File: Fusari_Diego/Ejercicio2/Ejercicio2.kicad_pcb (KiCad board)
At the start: 2 copper layers, 40.6 x 61 mm, 15 parts, among them J1 DB9, U1 AMIS42665TJAA1RG, U2 SP3232_V2

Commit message: Se agregan los archivos pcb con 3d
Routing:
- net GND: track 0.13 -> 20.2 mm, vias 0 -> 2
- added copper zone on B.Cu, net GND
- added copper zone on F.Cu, net GND
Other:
- board text added: "INDUSTRIA ARGENTINA"
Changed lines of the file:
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@@
   (general
     (links 43)
-    (no_connects 18)
+    (no_connects 0)
     (area 99.670799 78.664999 140.460801 139.775001)
     (thickness 1.6)
-    (drawings 4)
-    (tracks 205)
+    (drawings 5)
+    (tracks 215)
     (zones 0)
     (modules 15)
@@
     (user_trace_width 0.3048)
     (trace_clearance 0.3048)
-    (zone_clearance 0.508)
+    (zone_clearance 0.3048)
     (zone_45_only no)
     (trace_min 0.2)
@@
     (pad 2 smd rect (at 2 0) (size 2 1.7) (layers F.Cu F.Paste F.Mask)
       (net 20 "Net-(R1-Pad2)"))
-    (model Resistors_SMD.3dshapes/R_1206_HandSoldering.wrl
+    (model ${KIPRJMOD}/ej2.3dshapes/R_1206_HandSoldering.wrl
       (at (xyz 0 0 0))
       (scale (xyz 1 1 1))
@@
     (pad 2 smd rect (at 2 0) (size 2 1.7) (layers F.Cu F.Paste F.Mask)
       (net 10 "Net-(CAN1-Pad2)"))
-    (model Resistors_SMD.3dshapes/R_1206_HandSoldering.wrl
+    (model ${KIPRJMOD}/ej2.3dshapes/R_1206_HandSoldering.wrl
       (at (xyz 0 0 0))
       (scale (xyz 1 1 1))
@@
     (pad 16 smd rect (at -4.445 -2.59842 270) (size 0.59944 2.19964) (layers F.Cu F.Paste F.Mask)
       (net 9 +3.3V))
-    (model ${KIPRJMOD}/ej2.3dshapes/so-16.wrl
+    (model ${KIPRJMOD}/ej2.3dshapes/soic-16.wrl
       (at (xyz 0 0 0))
       (scale (xyz 1 1 1))
@@
     (pad 2 smd rect (at 2.032 0 270) (size 2 1.6) (layers F.Cu F.Paste F.Mask)
       (net 2 "Net-(C1-Pad2)"))
+    (model ${KIPRJMOD}/ej2.3dshapes/C_1206_HandSoldering.wrl
+      (at (xyz 0 0 0))
+      (scale (xyz 1 1 1))
+      (rotate (xyz 0 0 0))
+    )
   )
   (module ej2:C_1206_HandSoldering (layer F.Cu)
@@
     (pad 2 smd rect (at 2.032 0 270) (size 2 1.6) (layers F.Cu F.Paste F.Mask)
       (net 4 "Net-(C2-Pad2)"))
+    (model ${KIPRJMOD}/ej2.3dshapes/C_1206_HandSoldering.wrl
+      (at (xyz 0 0 0))
+      (scale (xyz 1 1 1))
+      (rotate (xyz 0 0 0))
+    )
   )
   (module ej2:C_1206_HandSoldering (layer F.Cu)
@@
     (pad 2 smd rect (at 2.032 0 270) (size 2 1.6) (layers F.Cu F.Paste F.Mask)
       (net 6 "Net-(C3-Pad2)"))
+    (model ${KIPRJMOD}/ej2.3dshapes/C_1206_HandSoldering.wrl
+      (at (xyz 0 0 0))
+      (scale (xyz 1 1 1))
+      (rotate (xyz 0 0 0))
+    )
   )
   (module ej2:C_1206_HandSoldering (layer F.Cu)
@@
     (pad 2 smd rect (at 2.032 0) (size 2 1.6) (layers F.Cu F.Paste F.Mask)
       (net 7 "Net-(C4-Pad2)"))
+    (model ${KIPRJMOD}/ej2.3dshapes/C_1206_HandSoldering.wrl
+      (at (xyz 0 0 0))
+      (scale (xyz 1 1 1))
+      (rotate (xyz 0 0 0))
+    )
   )
   (module ej2:C_1206_HandSoldering (layer F.Cu)
@@
     (pad 2 smd rect (at 2.032 0 180) (size 2 1.6) (layers F.Cu F.Paste F.Mask)
       (net 8 "Net-(C5-Pad2)"))
+    (model ${KIPRJMOD}/ej2.3dshapes/C_1206_HandSoldering.wrl
+      (at (xyz 0 0 0))
+      (scale (xyz 1 1 1))
+      (rotate (xyz 0 0 0))
+    )
   )
   (module ej2:C_1206_HandSoldering (layer F.Cu)
@@
     (pad 2 smd rect (at 2.032 0) (size 2 1.6) (layers F.Cu F.Paste F.Mask)
       (net 1 GND))
+    (model ${KIPRJMOD}/ej2.3dshapes/C_1206_HandSoldering.wrl
+      (at (xyz 0 0 0))
+      (scale (xyz 1 1 1))
+      (rotate (xyz 0 0 0))
+    )
   )
   (module ej2:Logo_OSHWA (layer F.Cu)
@@
       (xy 3.778435 -0.1467) (xy 3.778435 -0.1467)) (layer F.SilkS) (width 0.1))
   )
+  (gr_text "INDUSTRIA ARGENTINA" (at 124.2822 138.2776) (layer B.Cu)
+    (effects (font (size 1.5 1.5) (thickness 0.3)) (justify mirror))
+  )
   (gr_line (start 140.3858 139.7) (end 140.3858 78.74) (angle 90) (layer Edge.Cuts) (width 0.15))
   (gr_line (start 99.7458 139.7) (end 140.3858 139.7) (angle 90) (layer Edge.Cuts) (width 0.15))
   (gr_line (start 99.7458 78.74) (end 99.7458 139.7) (angle 90) (layer Edge.Cuts) (width 0.15))
   (gr_line (start 140.3858 78.74) (end 99.7458 78.74) (angle 90) (layer Edge.Cuts) (width 0.15))
+  (via (at 125.8824 103.9368) (size 1.27) (drill 0.7112) (layers F.Cu B.Cu) (net 1))
+  (segment (start 123.19762 103.9368) (end 125.8824 103.9368) (width 0.3048) (layer F.Cu) (net 1))
+  (segment (start 113.8936 121.6914) (end 111.2078 121.6914) (width 0.3048) (layer F.Cu) (net 1))
+  (segment (start 111.2078 121.6914) (end 111.1758 121.7234) (width 0.3048) (layer F.Cu) (net 1))
+  (segment (start 113.3602 124.5108) (end 113.8936 123.9774) (width 0.3048) (layer B.Cu) (net 1))
+  (segment (start 113.8936 123.9774) (end 113.8936 121.6914) (width 0.3048) (layer B.Cu) (net 1))
+  (via (at 113.8936 121.6914) (size 1.27) (drill 0.7112) (layers F.Cu B.Cu) (net 1))
+  (segment (start 103.5558 124.5108) (end 113.3602 124.5108) (width 0.3048) (layer B.Cu) (net 1))
+  (segment (start 103.124 122.8852) (end 103.124 124.079) (width 0.3048) (layer B.Cu) (net 1))
+  (segment (start 103.124 124.079) (end 103.5558 124.5108) (width 0.3048) (layer B.Cu) (net 1))
   (segment (start 116.84 88.5632) (end 116.745 88.4682) (width 0.3048) (layer F.Cu) (net 1))
   (segment (start 111.1758 125.7554) (end 113.665 125.7554) (width 0.3048) (layer F.Cu) (net 2))
@@
   (via (at 125.8824 107.7976) (size 1.27) (drill 0.7112) (layers F.Cu B.Cu) (net 26))
   (segment (start 125.8316 107.7468) (end 125.8824 107.7976) (width 0.3048) (layer F.Cu) (net 26))
+  (zone (net 1) (net_name GND) (layer F.Cu) (hatch full 0.508)
+    (connect_pads (clearance 0.3048))
+    (min_thickness 0.3048)
+    (fill yes (arc_segments 32) (thermal_gap 0.3048) (thermal_bridge_width 0.508))
+    (polygon
+      (pts
+        (xy 140.3858 78.74) (xy 140.3604 139.6746) (xy 99.7458 139.6746) (xy 99.7204 78.7146) (xy 99.7458 78.7146)
+        (xy 140.3858 78.74)
+      )
+    )
+  )
+  (zone (net 1) (net_name GND) (layer B.Cu) (hatch full 0.508)
+    (connect_pads (clearance 0.3048))
+    (min_thickness 0.3048)
+    (fill yes (arc_segments 32) (thermal_gap 0.3048) (thermal_bridge_width 0.508))
+    (polygon
+      (pts
+        (xy 99.7204 78.7146) (xy 140.3604 78.74) (xy 140.3604 139.7) (xy 99.7458 139.6746)
+      )
+    )
+  )
+  (zone (net 0) (net_name "") (layer F.Cu) (hatch full 0.508)
+    (connect_pads (clearance 0.3048))
+    (min_thickness 0.3048)
+    (keepout (tracks allowed) (vias allowed) (copperpour not_allowed))
+    (fill yes (arc_segments 32) (thermal_gap 0.3048) (thermal_bridge_width 0.508))
+    (polygon
+      (pts
+        (xy 100.7364 115.5954) (xy 105.283 115.5446) (xy 105.3338 125.7554) (xy 101.1174 125.8062)
+      )
+    )
+  )
+  (zone (net 0) (net_name "") (layer B.Cu) (hatch full 0.508)
+    (connect_pads (clearance 0.3048))
+    (min_thickness 0.3048)
+    (keepout (tracks allowed) (vias allowed) (copperpour not_allowed))
+    (fill yes (arc_segments 32) (thermal_gap 0.3048) (thermal_bridge_width 0.508))
+    (polygon
+      (pts
+        (xy 100.8634 115.7478) (xy 105.1814 115.7732) (xy 105.1052 124.6632) (xy 100.965 124.6632) (xy 100.838 115.7478)
+      )
+    )
+  )
+  (zone (net 0) (net_name "") (layer B.Cu) (hatch full 0.508)
+    (connect_pads (clearance 0.3048))
+    (min_thickness 0.3048)
+    (keepout (tracks allowed) (vias allowed) (copperpour not_allowed))
+    (fill yes (arc_segments 32) (thermal_gap 0.3048) (thermal_bridge_width 0.508))
+    (polygon
+      (pts
+        (xy 111.0234 137.0076) (xy 137.5156 137.033) (xy 137.4394 139.2174) (xy 111.125 139.2936) (xy 110.998 136.9822)
+      )
+    )
+  )
 )

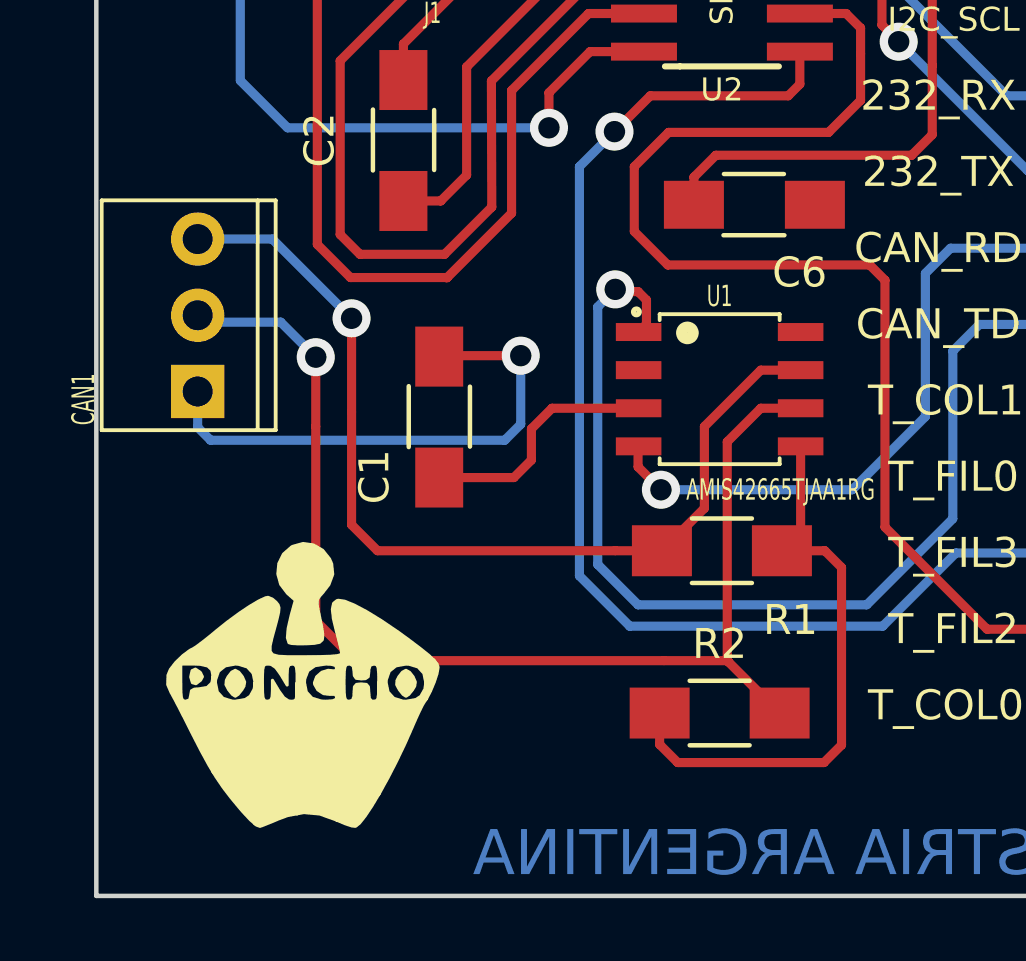
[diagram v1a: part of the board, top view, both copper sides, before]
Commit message: Se agrega modificacion de pcb y license
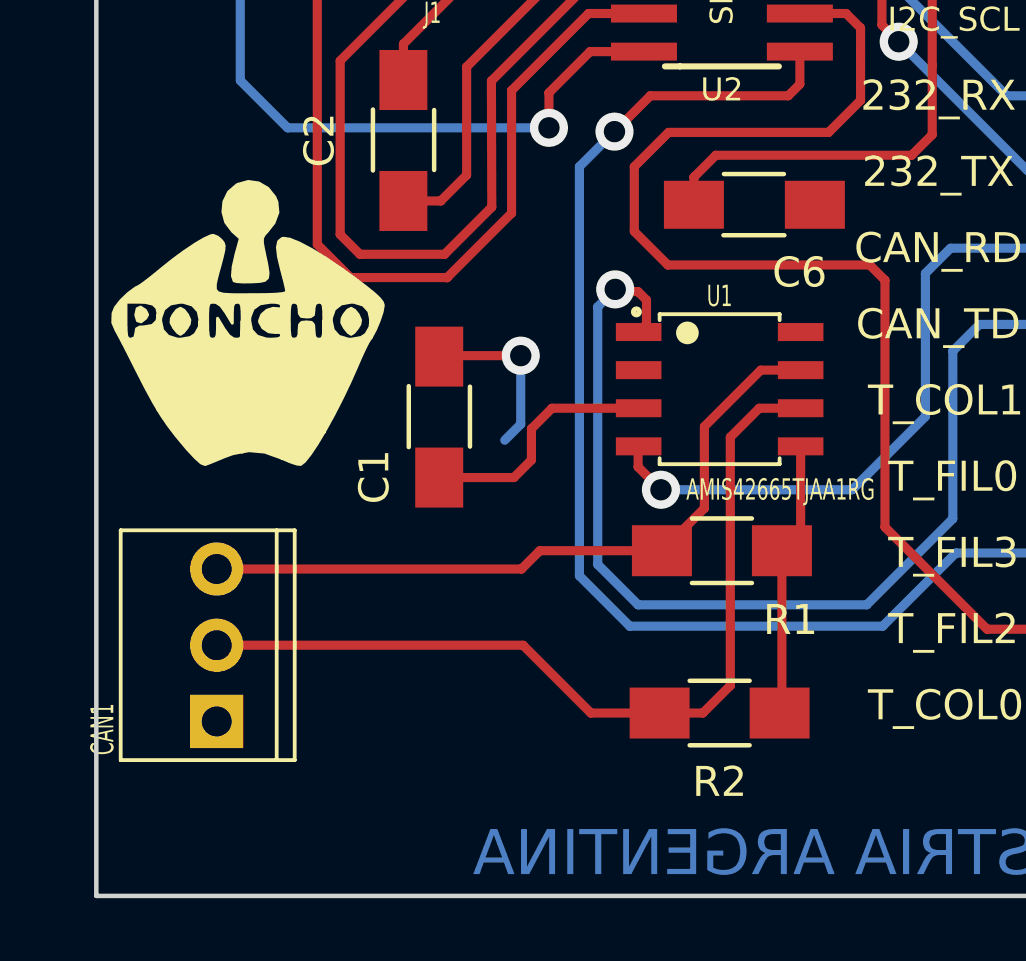
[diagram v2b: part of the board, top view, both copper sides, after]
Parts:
- moved ? 12.2 mm to (104.8, 120.7)
- moved CAN1 11.0 mm to (103.8, 131.3)
- turned R2 to 180 degrees
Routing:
- net GND: track 20.2 -> 8.59 mm
- net Net-(CAN1-Pad2): track 40.2 -> 29.7 mm, vias 1 -> 0
- net Net-(R1-Pad2): track 19.5 -> 9.18 mm
- net Net-(CAN1-Pad3): track 32.5 -> 23.8 mm, vias 1 -> 0

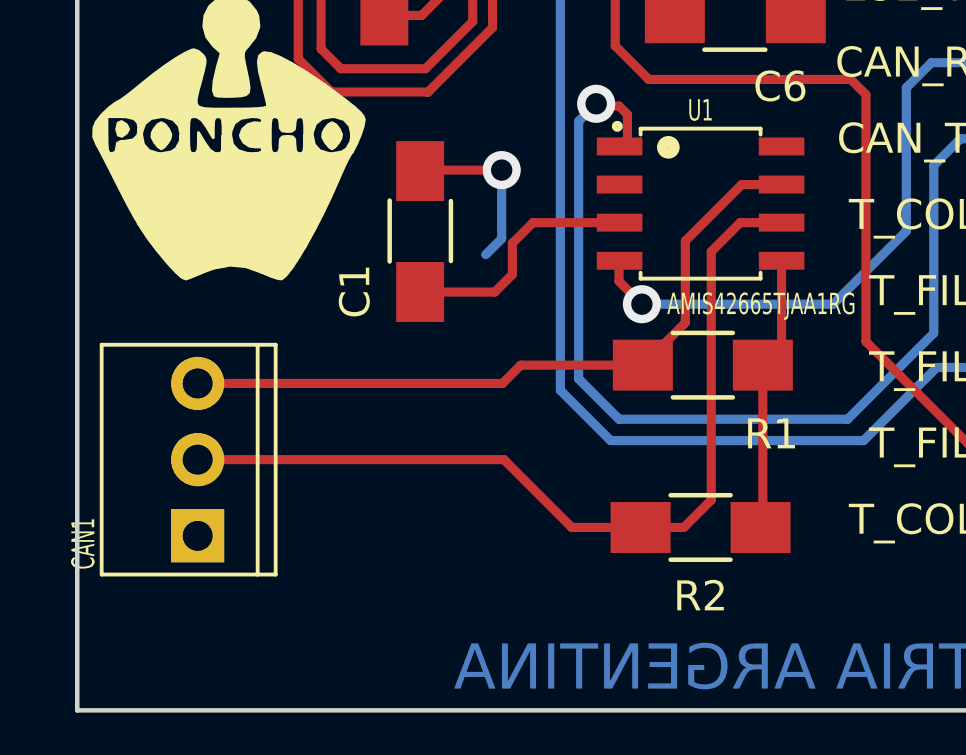
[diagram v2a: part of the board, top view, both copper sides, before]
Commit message: Al pcb se le agregaron los controles de impedancias
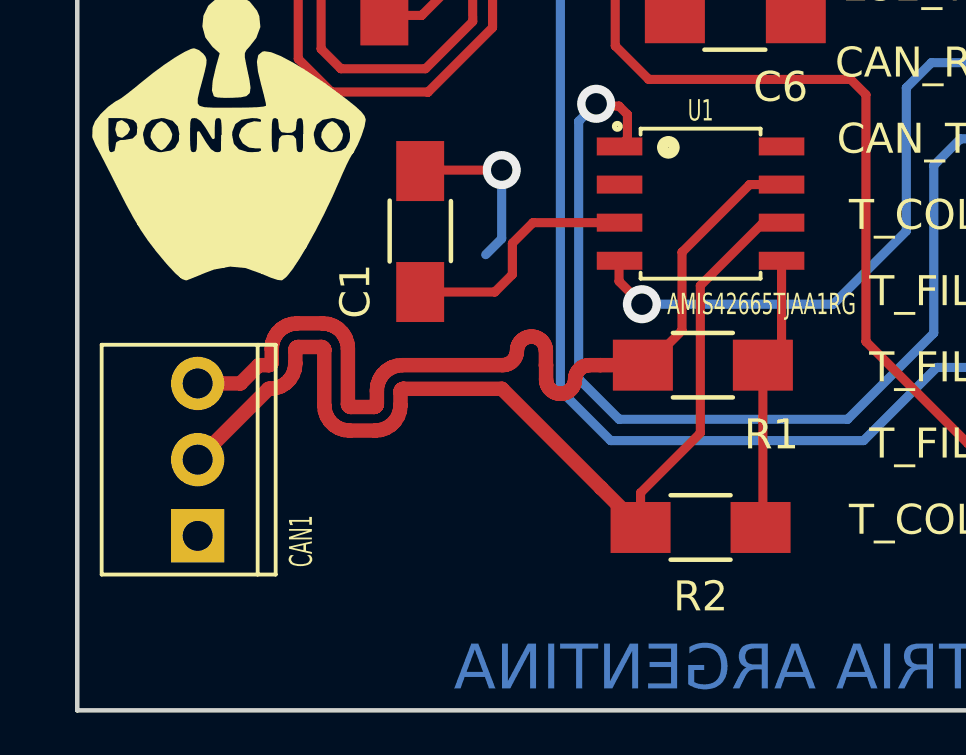
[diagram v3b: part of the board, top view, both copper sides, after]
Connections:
- net Net-(CAN1-Pad2) renamed /Conector y CAN/CAN_N
- net Net-(CAN1-Pad3) renamed /Conector y CAN/CAN_P
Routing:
- net /Conector y CAN/CAN_P: track 23.8 -> 30.7 mm
- net /Conector y CAN/CAN_N: track 29.7 -> 34.7 mm
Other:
- copper layers 2 -> 4
- board text added: "---------"
- board text added: "1 oz"
- board text added: "L1 Top (signal) L2 GND (Plane)"
- board text added: "L3 PWR (Mixed) L4 Bottom (Signal)"
- board text added: "Prepeg isola 2 x 762BAT05 Laminate isola 4 x 762BM Prepeg isola 2 x 762BAT05"
- board text added: "Stack-UP:"
- board text added: "Terminaciòn superficial: HASL Espesor final aproximado: 1,6mm"
